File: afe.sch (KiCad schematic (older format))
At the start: 56 parts, among them J2 Conn_01x05, Q5 2N7002, Q6 2N7002, Q8 2N7002, Q9 2N7002, U10 TS5A2053, U11 ADS7946SRTET, U13 USBLC6-2SC6, U5 REF2915, U6 TCA9535MRGER, U7 TLV9062S, U8 OPA2322S, U9 TS5A2053

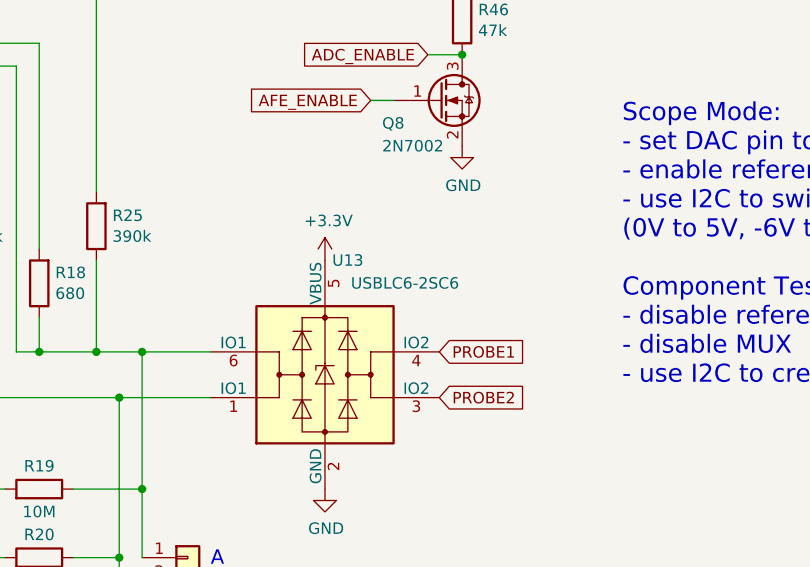
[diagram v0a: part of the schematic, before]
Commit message: added datasheets and descriptions
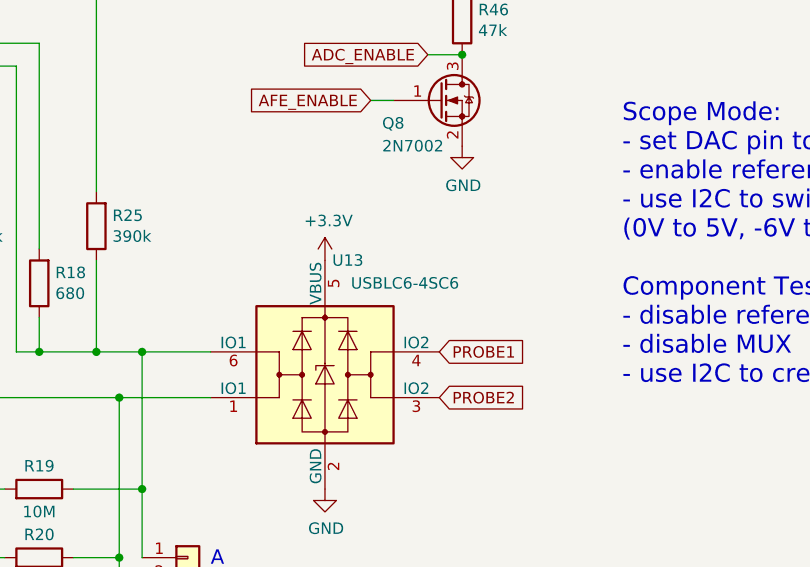
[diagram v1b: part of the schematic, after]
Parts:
- U13: value USBLC6-2SC6 -> USBLC6-4SC6
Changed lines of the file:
@@
 F 1 "ADS7946SRTET" H 9400 3229 50  0000 C CNN
 F 2 "Package_DFN_QFN:QFN-16-1EP_3x3mm_P0.5mm_EP1.8x1.8mm" H 9400 1950 50  0001 L BNN
-F 3 "ADS7946SRTET" H 9400 1950 50  0001 L BNN
+F 3 "http://www.ti.com/lit/ds/symlink/ads7946.pdf" H 9400 1950 50  0001 L BNN
 F 4 "WFQFN-16 Texas Instruments" H 9400 1950 50  0001 L BNN "Field4"
 F 5 "Unavailable" H 9400 1950 50  0001 L BNN "Field5"
@@
 P 5400 4900
 F 0 "U13" H 5500 5400 50  0000 C CNN
-F 1 "USBLC6-2SC6" H 5750 5300 50  0000 C CNN
+F 1 "USBLC6-4SC6" H 5750 5300 50  0000 C CNN
 F 2 "Package_TO_SOT_SMD:SOT-23-6" H 4650 5300 50  0001 C CNN
 F 3 "http://www2.st.com/resource/en/datasheet/CD00050750.pdf" H 5600 5250 50  0001 C CNN

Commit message: add anotation
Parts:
- C6: footprint (none) -> Capacitor_SMD:C_0603_1608Metric
- FB1: footprint (none) -> Inductor_SMD:L_0603_1608Metric
- LS1: footprint (none) -> Connector_PinHeader_1.00mm:PinHeader_1x02_P1.00mm_Vertical
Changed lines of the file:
@@
 F 0 "FB1" V 8313 1050 50  0000 C CNN
 F 1 "Ferret" V 8404 1050 50  0000 C CNN
-F 2 "" V 8480 1050 50  0001 C CNN
+F 2 "Inductor_SMD:L_0603_1608Metric" V 8480 1050 50  0001 C CNN
 F 3 "~" H 8550 1050 50  0001 C CNN
 	1    8550 1050
@@
 F 0 "C6" H 1888 6946 50  0000 L CNN
 F 1 "4u7" H 1888 6855 50  0000 L CNN
-F 2 "" H 1800 6900 50  0001 C CNN
+F 2 "Capacitor_SMD:C_0603_1608Metric" H 1800 6900 50  0001 C CNN
 F 3 "~" H 1800 6900 50  0001 C CNN
 	1    1800 6900
@@
 F 0 "LS1" H 2420 7046 50  0000 L CNN
 F 1 "Speaker" H 2420 6955 50  0000 L CNN
-F 2 "" H 2250 6850 50  0001 C CNN
+F 2 "Connector_PinHeader_1.00mm:PinHeader_1x02_P1.00mm_Vertical" H 2250 6850 50  0001 C CNN
 F 3 "~" H 2240 7000 50  0001 C CNN
 	1    2250 7050

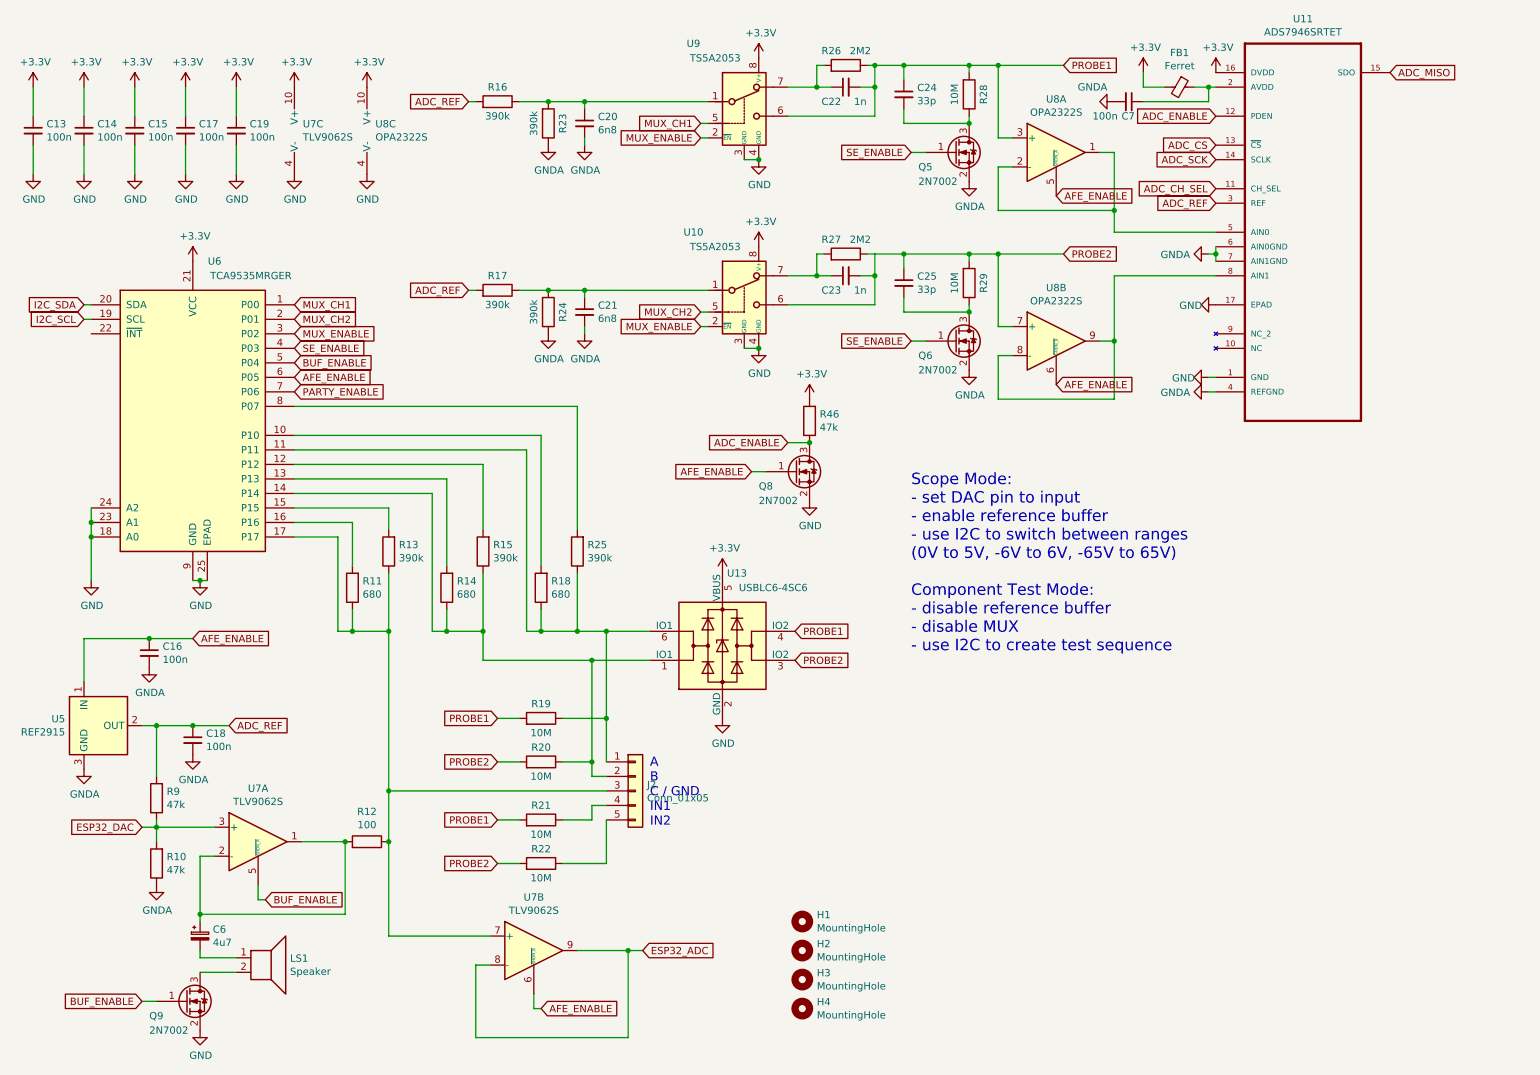
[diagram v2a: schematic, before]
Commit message: UPD: finalized schematic, started layout
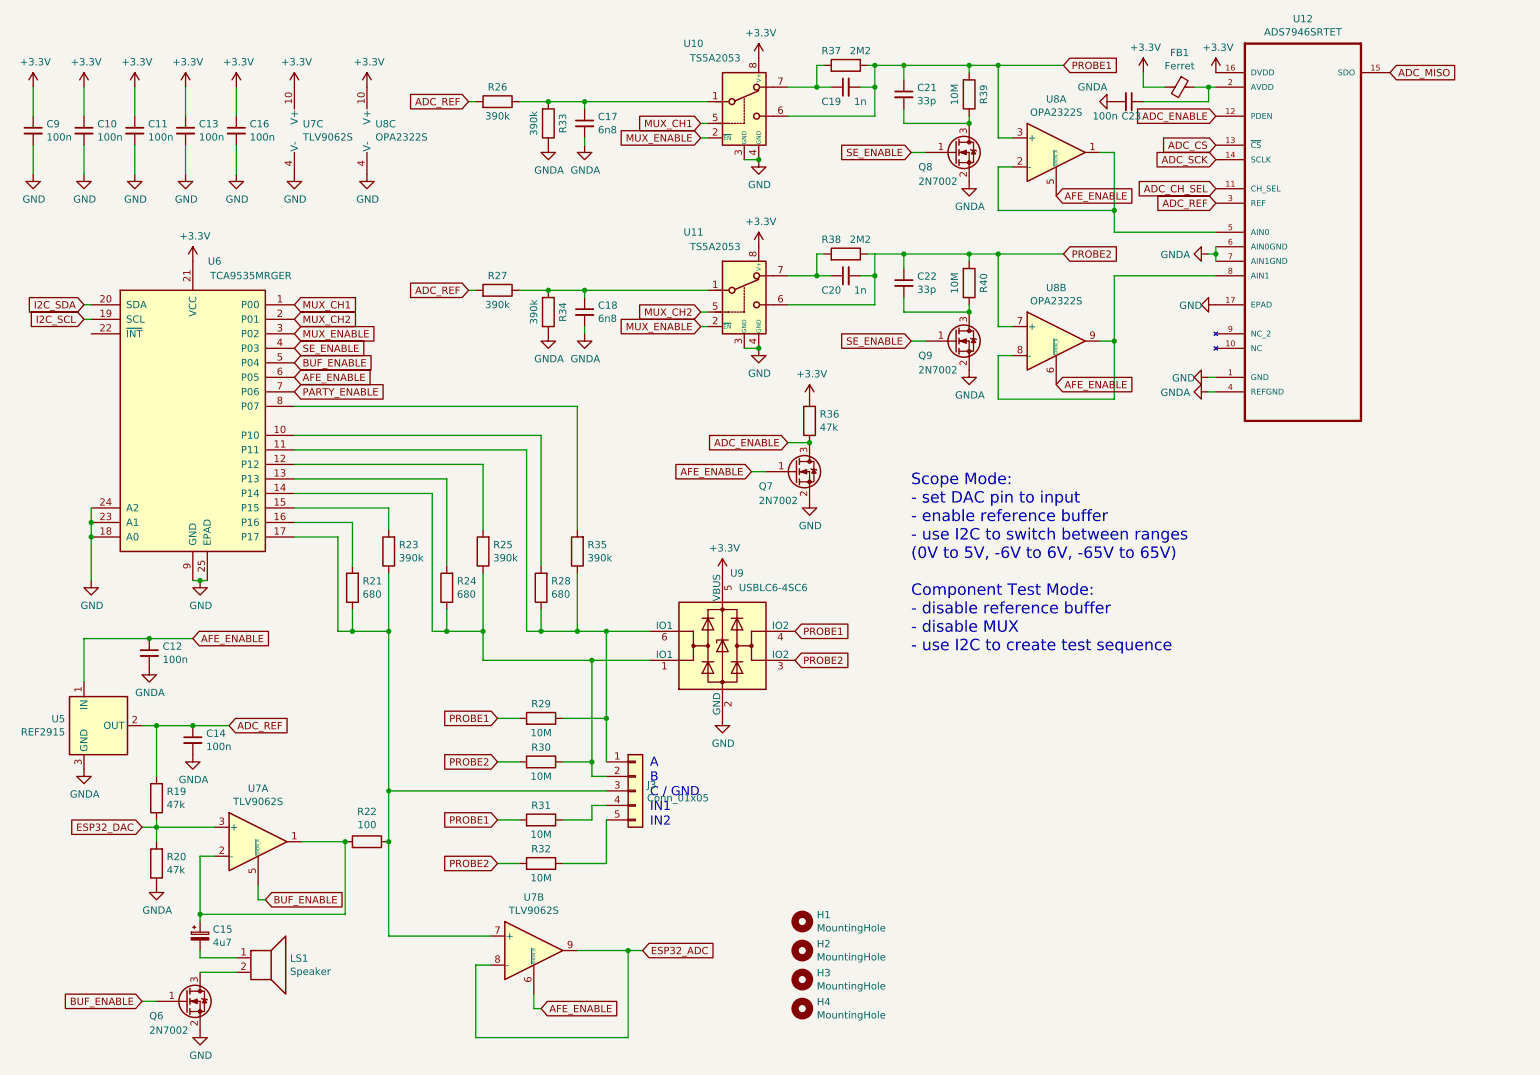
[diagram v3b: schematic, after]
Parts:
- LS1: footprint Connector_PinHeader_1.00mm:PinHeader_1x02_P1.00mm_Vertical -> Connector_Molex:Molex_KK-254_AE-6410-02A_1x02_P2.54mm_Vertical
- renumbered C14 to C10, C15 to C11, C16 to C12, C17 to C13, C18 to C14, C6 to C15, C19 to C16, C20 to C17, C21 to C18, C22 to C19, C23 to C20, C24 to C21, C25 to C22, C7 to C23, C13 to C9, J2 to J3, Q9 to Q6, Q8 to Q7, Q5 to Q8, Q6 to Q9, R9 to R19, R10 to R20, R11 to R21, R12 to R22, R13 to R23, R14 to R24, R15 to R25, R16 to R26, R17 to R27, R18 to R28, R19 to R29, R20 to R30, R21 to R31, R22 to R32, R23 to R33, R24 to R34, R25 to R35, R46 to R36, R26 to R37, R27 to R38, R28 to R39, R29 to R40, U9 to U10, U10 to U11, U11 to U12, U13 to U9

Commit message: ADD: constant current source for high power LED
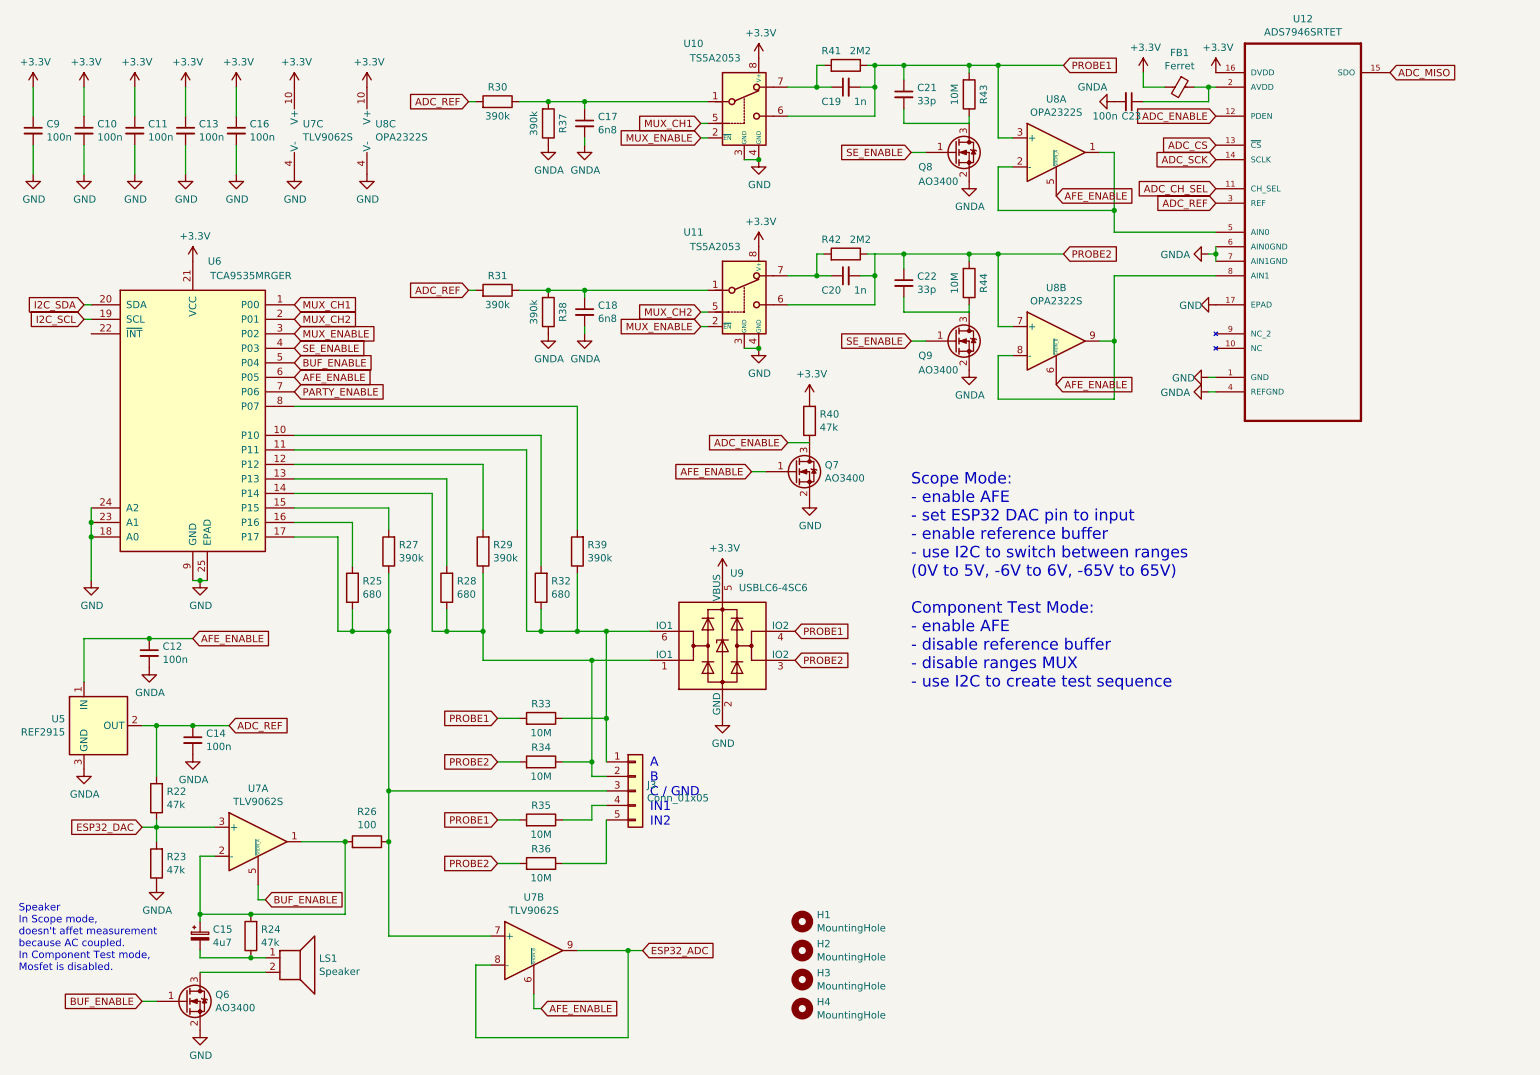
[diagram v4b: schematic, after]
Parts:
- removed Q6, Q7, Q8, Q9: 2N7002, Package_TO_SOT_SMD:SOT-23, symbol Transistor_FET:2N7002
- added Q6, Q7, Q8, Q9: AO3400, Package_TO_SOT_SMD:SOT-23, symbol Device:Q_NMOS_GSD
- added R24: 47k, Resistor_SMD:R_0603_1608Metric, symbol Device:R
- renumbered R19 to R22, R20 to R23, R21 to R25, R22 to R26, R23 to R27, R24 to R28, R25 to R29, R26 to R30, R27 to R31, R28 to R32, R29 to R33, R30 to R34, R31 to R35, R32 to R36, R33 to R37, R34 to R38, R35 to R39, R36 to R40, R37 to R41, R38 to R42, R39 to R43, R40 to R44
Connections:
- net ADC_ENABLE: now also Q7.3 (D)
- net AFE_ENABLE: now also Q7.1 (G)
- net BUF_ENABLE: now also Q6.1 (G)
- net GND: now also Q6.2 (S), Q7.2 (S)
- net GNDA: now also Q8.2 (S), Q9.2 (S)
- net SE_ENABLE: now also Q8.1 (G), Q9.1 (G)
- net at C15.1, R26.2, U7.1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: now also R24.2
- net at C21.2, R43.1: now also Q8.3 (D)
- net at C22.2, R44.1: now also Q9.3 (D)
- net at C15.2, LS1.1: now also R24.1
- net at LS1.2: now also Q6.3 (D)
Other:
- note added: "Scope Mode:\n- enable AFE\n- set ESP32 DAC pin to input\n- enable reference buffer\n- use I2C to switch between ranges\n(0V to 5V, -6V to 6V, -65V to 65V)\n\nComponent Test Mode:\n- enable AFE\n- disable reference buffer\n- disable ranges MUX\n- use I2C to create test sequence"
- note added: "Speaker\nIn Scope mode, \ndoesn't affet measurement \nbecause AC coupled.\nIn Component Test mode, \nMosfet is disabled."
- note removed: "Scope Mode:\n- set DAC pin to input\n- enable reference buffer\n- use I2C to switch between ranges\n(0V to 5V, -6V to 6V, -65V to 65V)\n\nComponent Test Mode:\n- disable reference buffer\n- disable MUX\n- use I2C to create test sequence"
- moved on the sheet: LS1
